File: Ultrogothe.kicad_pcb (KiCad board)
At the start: 2 copper layers, 54 parts, among them J1 Conn_01x20, J2 Conn_01x20, J3 Conn_ARM_SWD_TagConnect_TC203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, J4 USB_C_Receptacle, Q1 S9013, U1 STM32F103CBTx, U2 XC6206PxxxMR, U3 STM32F103CBTx, Y1 Crystal, Y2 Crystal

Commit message: pcb : mise en place pour forme en cours
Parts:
- moved J3 83.8 mm to (63.3, 72.2)
- moved JP2 83.8 mm to (49.4, 80.6)
- moved JP3 83.8 mm to (49.4, 84.2)
- moved JP4 83.8 mm to (49.4, 87.7)
- moved JP5 83.8 mm to (49.4, 91.2)
- moved JP6 83.8 mm to (49.4, 94.8)
- moved JP7 83.8 mm to (49.4, 98.3)
- moved JP8 83.8 mm to (49.4, 101.9)
- moved R10 83.8 mm to (57.3, 55.5)
- moved R11 83.8 mm to (57.3, 58.0)
- moved R12 83.8 mm to (57.3, 60.5)
- moved R13 83.8 mm to (57.3, 63.0)
- moved R14 83.8 mm to (57.3, 65.5)
- moved R8 83.8 mm to (57.3, 50.4)
- moved R9 83.8 mm to (57.3, 52.9)
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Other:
- board outline added: 20.3 x 54.6 mm

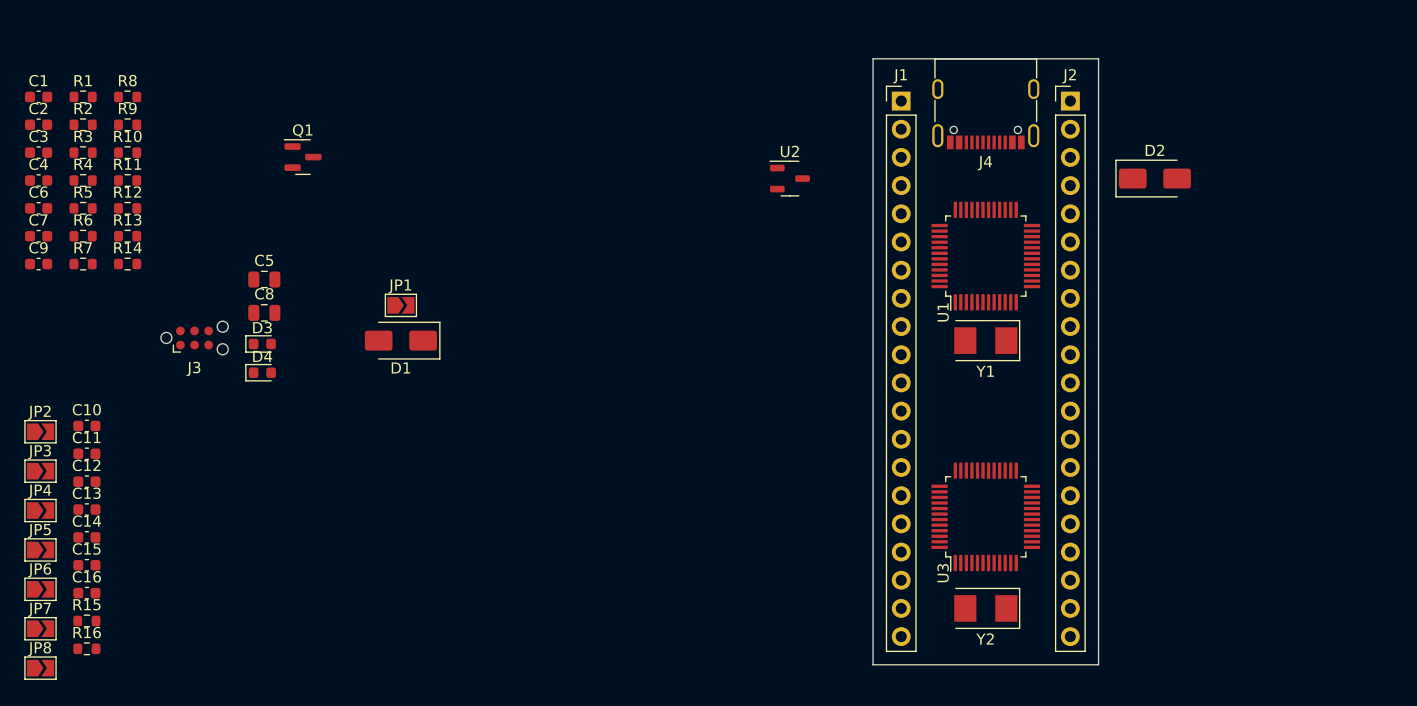
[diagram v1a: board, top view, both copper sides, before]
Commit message: passif en 0402
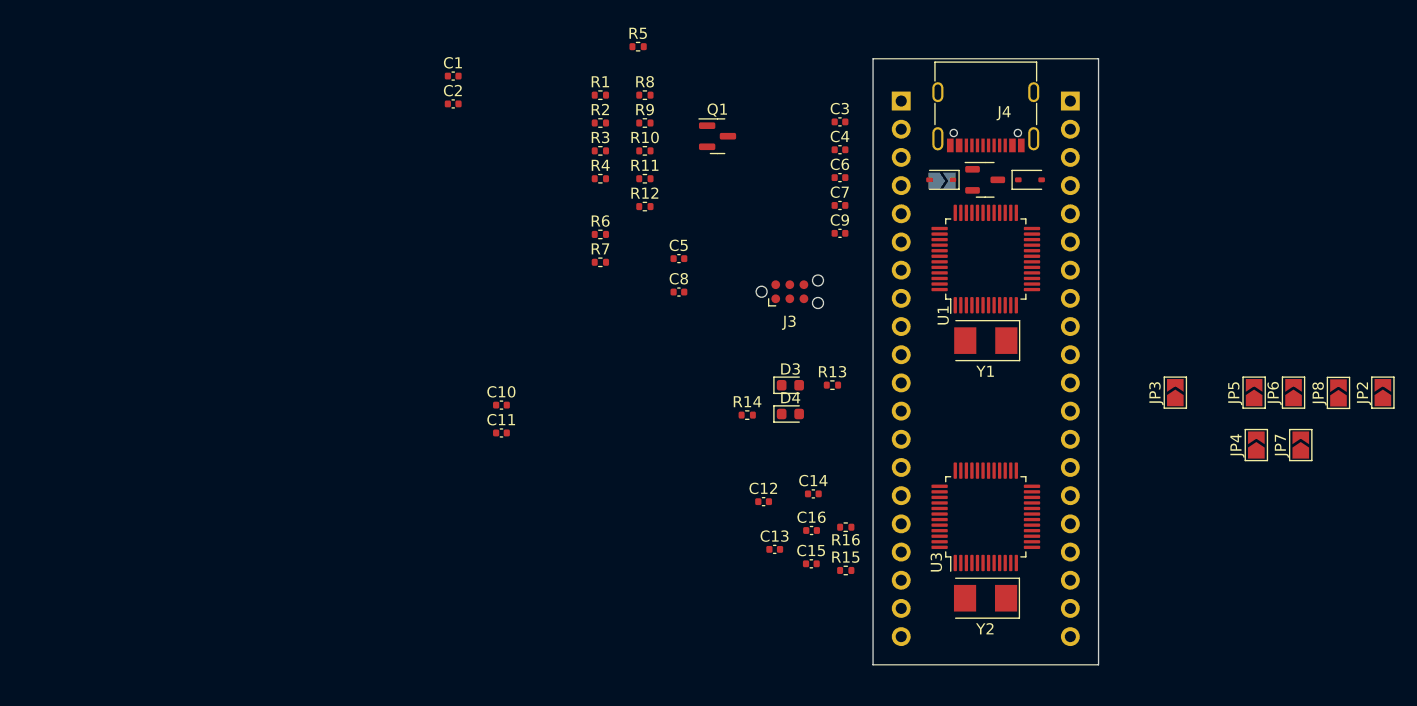
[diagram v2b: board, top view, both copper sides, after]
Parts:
- C1, C10, C11, C12, C13, C14, C15, C16, C2, C3, C4, C6, C7, C9: footprint Capacitor_SMD:C_0603_1608Metric -> Capacitor_SMD:C_0402_1005Metric
- C5, C8: value 10uF -> 1uF; footprint Capacitor_SMD:C_0805_2012Metric -> Capacitor_SMD:C_0402_1005Metric
- D1, D2: value SS14 -> 1N5819WS; footprint Diode_SMD:D_SMA -> Diode_SMD:D_SOD-323
- J1, J2, JP1: moved to B.Cu
- R1, R10, R11, R12, R13, R14, R15, R16, R2, R3, R4, R5, R6, R7, R8: footprint Resistor_SMD:R_0603_1608Metric -> Resistor_SMD:R_0402_1005Metric
- R9: value 36k -> 39k; footprint Resistor_SMD:R_0603_1608Metric -> Resistor_SMD:R_0402_1005Metric
- moved JP2 121.0 mm to (170.4, 77.1), turned to 90 degrees
- moved JP8 119.6 mm to (166.4, 77.1), turned to 90 degrees
- moved JP7 114.8 mm to (163.0, 81.8), turned to 90 degrees
- moved JP6 114.3 mm to (162.3, 77.1), turned to 90 degrees
- moved JP5 110.3 mm to (158.8, 77.1), turned to 90 degrees
- moved JP4 109.7 mm to (159.0, 81.8), turned to 90 degrees
- moved JP3 102.5 mm to (151.7, 77.1), turned to 90 degrees
- moved C3 72.3 mm to (121.5, 52.7)
- moved C4 72.3 mm to (121.5, 55.2)
- moved C6 72.3 mm to (121.5, 57.7)
- moved C7 72.3 mm to (121.5, 60.2)
- moved C9 72.3 mm to (121.5, 62.7)
- moved R16 69.3 mm to (122.0, 89.2), turned to 180 degrees
- moved R15 68.5 mm to (122.0, 93.1)
- moved C14 65.6 mm to (119.1, 86.2)
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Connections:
- C3 pad 1: 0V -> /s_debugger/nRST
- C3 pad 2: /s_debugger/nRST -> 0V
- R10 pad 1: /s_debugger/RENUM -> Net-(Q1-B)
- R10 pad 2: Net-(Q1-B) -> /s_debugger/RENUM
- R8 pad 1: /s_debugger/VBUS -> Net-(Q1-B)
- R8 pad 2: Net-(Q1-B) -> /s_debugger/VBUS

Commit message: simplification
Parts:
- removed C1, C2: 20pF, Capacitor_SMD:C_0402_1005Metric
- removed C3, C4, C6, C7, C9: 100nF, Capacitor_SMD:C_0402_1005Metric
- removed D2: 1N5819WS, Diode_SMD:D_SOD-323
- removed D3: 19-217/BHC-ZL1M2RY/6T, LED_SMD:LED_0603_1608Metric
- removed D4: KT-0603R, LED_SMD:LED_0603_1608Metric
- removed J4: USB_C_Receptacle, Connector_USB:USB_C_Receptacle_G-Switch_GT-USB-7010ASV
- removed JP1: SolderJumper_2_Open, Jumper:SolderJumper-2_P1.3mm_Open_TrianglePad1.0x1.5mm
- removed Q1: S9013, Package_TO_SOT_SMD:SOT-23
- removed R1: 5k1, Resistor_SMD:R_0402_1005Metric
- removed R10, R4: 100, Resistor_SMD:R_0402_1005Metric
- removed R11, R12: 4k7, Resistor_SMD:R_0402_1005Metric
- removed R13, R14: 220, Resistor_SMD:R_0402_1005Metric
- removed R2, R3: 100k, Resistor_SMD:R_0402_1005Metric
- removed R5: 1k5, Resistor_SMD:R_0402_1005Metric
- removed R6, R7, R8: 10k, Resistor_SMD:R_0402_1005Metric
- removed R9: 39k, Resistor_SMD:R_0402_1005Metric
- removed U1: STM32F103CBTx, Package_QFP:LQFP-48_7x7mm_P0.5mm
- removed Y1: Crystal, Crystal:Crystal_SMD_5032-2Pin_5.0x3.2mm
- J3: value Conn_ARM_SWD_TagConnect_TC2030-NL -> Conn_02x05_Top_Bottom; footprint Connector:Tag-Connect_TC2030-IDC-NL_2x03_P1.27mm_Vertical -> Connector_PinSocket_2.00mm:PinSocket_2x05_P2.00mm_Horizontal
- moved J3 24.2 mm to (138.6, 57.2), turned to -90 degrees
- moved U3 14.0 mm to (134.6, 74.3)
- moved Y2 12.4 mm to (134.6, 83.2)
- moved C5 9.68 mm to (98.3, 69.3)
- moved C8 9.48 mm to (99.1, 73.3)
- moved U2 4.30 mm to (137.3, 61.2), turned to 180 degrees
- moved D1 3.42 mm to (131.5, 61.2)
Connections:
- J3 pad 1: 3V3 -> unconnected-(J3-Pin_1-Pad1)
- J3 pad 2: /s_debugger/DIO -> unconnected-(J3-Pin_2-Pad2)
- J3 pad 3: /s_debugger/nRST -> /s_debugger/T_DIO
- J3 pad 4: /s_debugger/CLK -> /s_debugger/T_CLK
- J3 pad 5: 0V -> /s_debugger/T_SWO
- J3 pad 6: unconnected-(J3-SWO-Pad6) -> 0V

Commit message: renumerotation
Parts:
- removed C10, C11: 20pF, Capacitor_SMD:C_0402_1005Metric
- removed C12, C13, C14, C15, C16: 100nF, Capacitor_SMD:C_0402_1005Metric
- removed JP8: SolderJumper_2_Open, Jumper:SolderJumper-2_P1.3mm_Open_TrianglePad1.0x1.5mm
- removed R15, R16: 100k, Resistor_SMD:R_0402_1005Metric
- removed U3: STM32F103CBTx, Package_QFP:LQFP-48_7x7mm_P0.5mm
- removed Y2: Crystal, Crystal:Crystal_SMD_5032-2Pin_5.0x3.2mm
- added C1: 1uF, Capacitor_SMD:C_0402_1005Metric, F.Cu at (113.8, 85.0)
- added C2: 1uF, Capacitor_SMD:C_0402_1005Metric, F.Cu at (113.8, 87.0)
- added C3: 20pF, Capacitor_SMD:C_0402_1005Metric, F.Cu at (108.7, 73.2)
- added C4: 20pF, Capacitor_SMD:C_0402_1005Metric, F.Cu at (108.7, 75.1)
- added C6: 100nF, Capacitor_SMD:C_0402_1005Metric, F.Cu at (108.7, 77.1)
- added C7: 100nF, Capacitor_SMD:C_0402_1005Metric, F.Cu at (108.7, 79.1)
- added C9: 100nF, Capacitor_SMD:C_0402_1005Metric, F.Cu at (108.7, 81.1)
- added JP1: SolderJumper_2_Open, Jumper:SolderJumper-2_P1.3mm_Open_TrianglePad1.0x1.5mm, F.Cu at (115.6, 61.0)
- added R1: 100k, Resistor_SMD:R_0402_1005Metric, F.Cu at (115.9, 78.0)
- added R2: 100k, Resistor_SMD:R_0402_1005Metric, F.Cu at (115.9, 80.0)
- added U1: XC6206PxxxMR, Package_TO_SOT_SMD:SOT-23-3, F.Cu at (109.8, 86.3)
- added Y1: Crystal, Crystal:Crystal_SMD_5032-2Pin_5.0x3.2mm, F.Cu at (113.7, 74.6)
- C5, C8: value 1uF -> 100nF
- U2: value XC6206PxxxMR -> STM32F103CBTx; footprint Package_TO_SOT_SMD:SOT-23-3 -> Package_QFP:LQFP-48_7x7mm_P0.5mm
- moved U2 13.3 mm to (134.6, 74.3), turned to 45 degrees
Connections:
- C5 pad 2: /s_debugger/5V -> Net-(JP1-A)
- JP2 pad 1: Net-(JP2-A) -> Net-(JP1-A)
- JP2 pad 2: /s_debugger/T_RST -> /s_uC/nRST
- JP3 pad 1: Net-(JP2-A) -> /s_uC/A2
- JP3 pad 2: /s_uC/nRST -> /s_debugger/T_RX
- JP4 pad 1: /s_uC/A2 -> /s_uC/A8
- JP4 pad 2: /s_debugger/T_RX -> /s_debugger/T_SWO
- JP5 pad 1: /s_uC/A8 -> /s_uC/A13
- JP5 pad 2: /s_debugger/T_SWO -> /s_debugger/T_DIO
- JP6 pad 1: /s_uC/A13 -> /s_uC/A3
- JP6 pad 2: /s_debugger/T_DIO -> /s_debugger/T_TX
- JP7 pad 1: /s_uC/A3 -> /s_uC/A14
- JP7 pad 2: /s_debugger/T_TX -> /s_debugger/T_CLK
- U2 pad 1: 0V -> 3V3
- U2 pad 2: 3V3 -> /s_uC/C13
- U2 pad 3: /s_debugger/5V -> /s_uC/C14

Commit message: placement
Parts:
- removed JP7: SolderJumper_2_Open, Jumper:SolderJumper-2_P1.3mm_Open_TrianglePad1.0x1.5mm
- JP1, JP2, JP3, JP4, JP5, JP6: moved to B.Cu
- moved C5 40.4 mm to (133.6, 89.1), turned to 90 degrees
- moved C8 38.7 mm to (137.1, 80.6), turned to 180 degrees
- moved JP2 38.4 mm to (136.0, 60.1)
- moved D1 33.7 mm to (131.8, 94.9)
- moved JP4 33.7 mm to (133.2, 60.1)
- moved C7 32.6 mm to (139.8, 69.4), turned to -90 degrees
- moved C4 30.0 mm to (136.3, 86.8)
- moved U1 28.7 mm to (136.3, 97.1), turned to 180 degrees
- moved C3 27.1 mm to (132.1, 86.8), turned to 180 degrees
- moved C9 26.7 mm to (131.8, 67.7), turned to -90 degrees
- moved JP5 26.2 mm to (138.8, 60.1)
- moved JP6 25.4 mm to (138.4, 68.6), turned to 180 degrees
- moved C2 24.8 mm to (137.5, 94.4)
- moved C1 23.4 mm to (135.2, 94.4), turned to 180 degrees
- moved C6 22.5 mm to (130.8, 80.9), turned to 90 degrees
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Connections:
- C5 pad 2: Net-(JP1-A) -> /s_uC/nRST
- JP1 pad 1: Net-(JP1-A) -> /s_uC/nRST
- JP2 pad 1: Net-(JP1-A) -> /s_uC/A14
- JP2 pad 2: /s_uC/nRST -> /s_debugger/T_CLK
- R1 pad 2: Net-(JP1-A) -> /s_uC/nRST
- R2 pad 2: /s_uC/B0 -> /s_uC/boot
- U2 pad 44: /s_uC/B0 -> /s_uC/boot
- U2 pad 7: Net-(JP1-A) -> /s_uC/nRST
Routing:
- net /s_debugger/T_TX: track 0.00 -> 17.3 mm
- net /s_debugger/T_CLK: track 0.00 -> 4.73 mm
- net 3V3: track 0.00 -> 4.38 mm
- net /s_uC/nRST: track 0.00 -> 3.48 mm, vias 0 -> 1
- net /s_uC/A3: track 0.00 -> 3.21 mm
- net /s_uC/A2: track 0.00 -> 3.14 mm
- net /s_debugger/T_DIO: track 0.00 -> 3.09 mm
- net 0V: track 0.00 -> 2.87 mm, vias 0 -> 2
- net /s_debugger/T_SWO: track 0.00 -> 2.72 mm
- net /s_debugger/T_RST: track 0.00 -> 2.22 mm
- net /s_uC/B5: track 0.00 -> 0.76 mm
- net /s_uC/B9: track 0.00 -> 0.57 mm
- net /s_uC/B6: track 0.00 -> 0.51 mm
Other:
- copper layers 2 -> 4

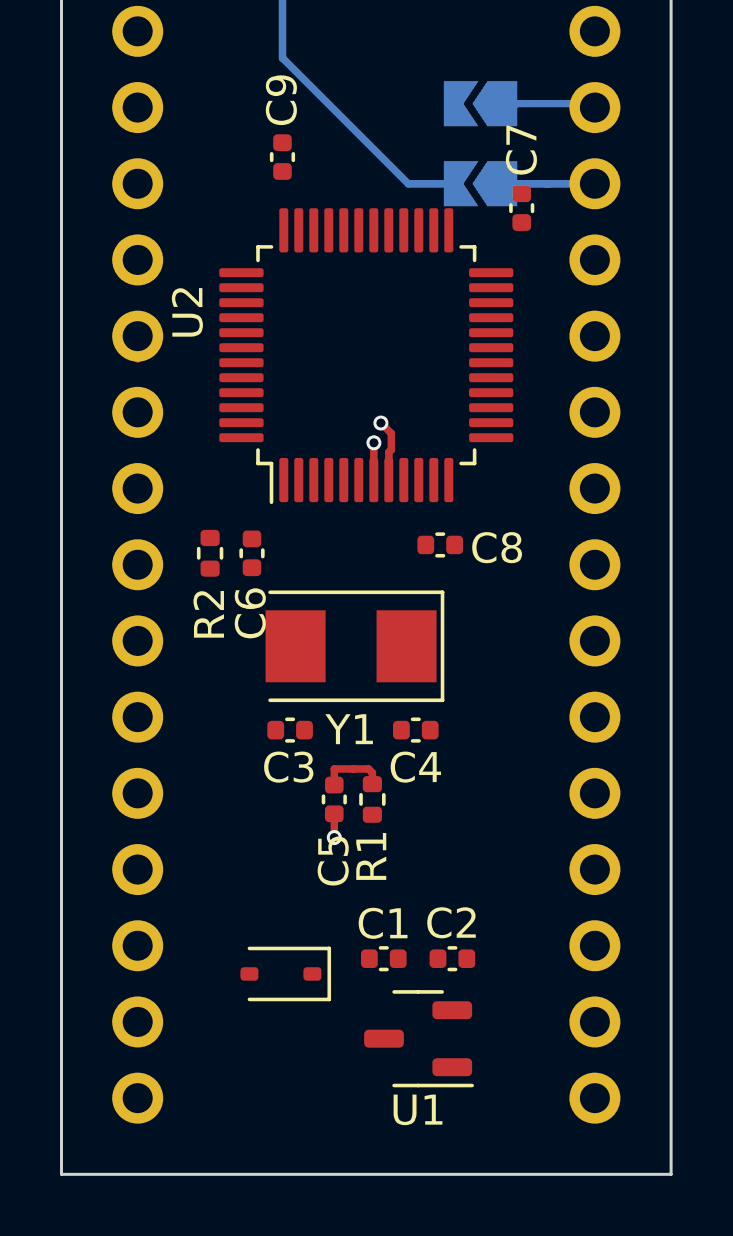
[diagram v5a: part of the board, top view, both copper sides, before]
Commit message: répartition pins encours
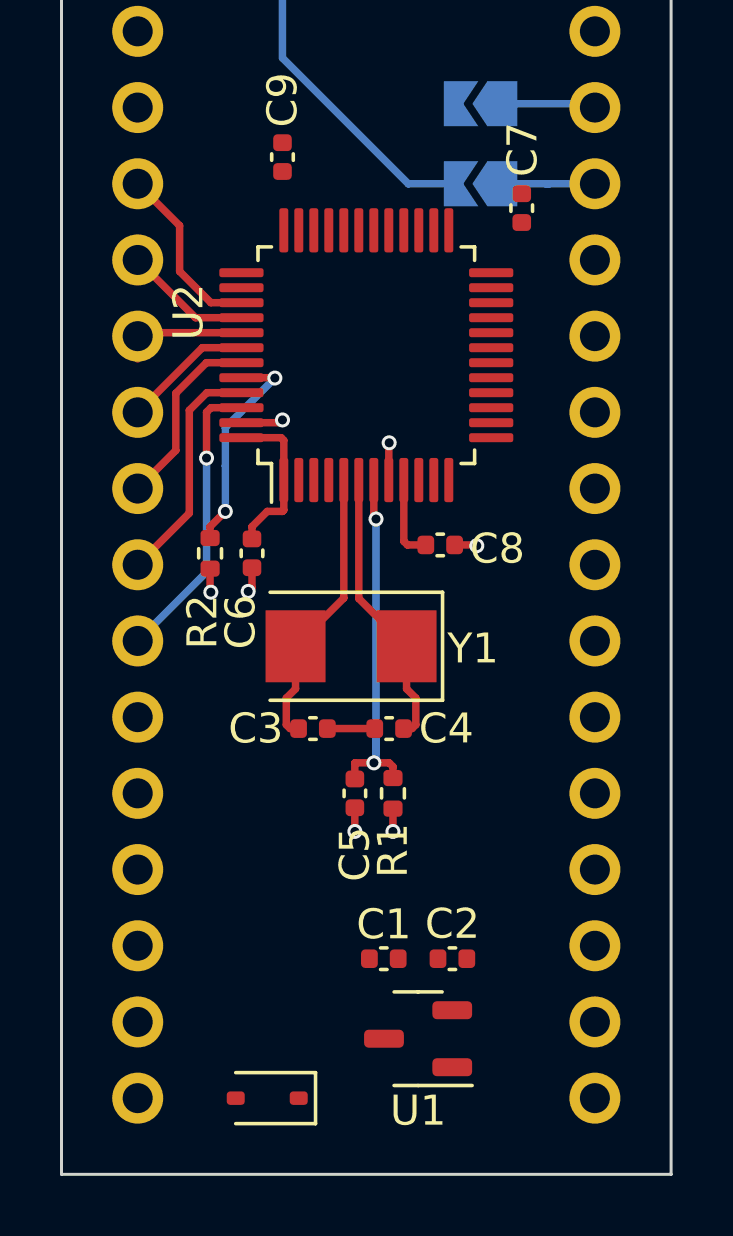
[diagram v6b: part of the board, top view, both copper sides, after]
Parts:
- moved D1 4.17 mm to (131.3, 99.1)
- moved C4 0.89 mm to (135.4, 86.7)
- moved C3 0.76 mm to (132.8, 86.7)
- moved C5 0.72 mm to (134.2, 88.9)
- moved R1 0.72 mm to (135.5, 88.9)
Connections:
- net /s_uC/A0 renamed A0
- net /s_uC/A1 renamed A1
- net /s_uC/A10 renamed A10
- net /s_uC/A11 renamed A11
- net /s_uC/A12 renamed A12
- net /s_uC/A13 renamed A13
- net /s_uC/A14 renamed A14
- net /s_uC/A15 renamed A15
- net /s_uC/A2 renamed A2
- net /s_uC/A3 renamed A3
- net /s_uC/A4 renamed A4
- net /s_uC/A5 renamed A5
- net /s_uC/A6 renamed A6
- net /s_uC/A7 renamed A7
- net /s_uC/A8 renamed A8
- net /s_uC/A9 renamed A9
- net /s_uC/B0 renamed B0
- net /s_uC/B1 renamed B1
- net /s_uC/B10 renamed B10
- net /s_uC/B11 renamed B11
- net /s_uC/B12 renamed B12
- net /s_uC/B13 renamed B13
- net /s_uC/B14 renamed B14
- net /s_uC/B15 renamed B15
- net /s_uC/B2 renamed B2
- net /s_uC/B3 renamed B3
- net /s_uC/B4 renamed B4
- net /s_uC/B5 renamed B5
- net /s_uC/B6 renamed B6
- net /s_uC/B7 renamed B7
- net /s_uC/B8 renamed B8
- net /s_uC/B9 renamed B9
- net /s_uC/C13 renamed C13
- net /s_uC/C14 renamed C14
- net /s_uC/C15 renamed C15
- net /s_uC/nRST renamed nRST
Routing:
- net B9: track 0.57 -> 10.4 mm, vias 0 -> 1
- net Net-(U2-PD0): track 0.00 -> 9.41 mm
- net Net-(U2-PD1): track 0.00 -> 9.41 mm
- net 3V3: track 4.38 -> 13.4 mm, vias 0 -> 1
- net nRST: track 3.48 -> 12.2 mm, vias 1 -> 2
- net B8: track 0.00 -> 7.84 mm
- net /s_uC/boot: track 0.00 -> 7.35 mm, vias 0 -> 2
- net B7: track 0.19 -> 6.31 mm
- net B3: track 0.00 -> 5.99 mm
- net 0V: track 2.87 -> 7.41 mm, vias 2 -> 6
- net B6: track 0.51 -> 4.86 mm
- net B4: track 0.00 -> 4.25 mm
- net B5: track 0.76 -> 4.27 mm
